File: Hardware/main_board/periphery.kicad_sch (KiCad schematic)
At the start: 66 parts, among them J4 SD, J5 NFC, J6 EXT1, J7 EXT0, U12 LP5562TMX

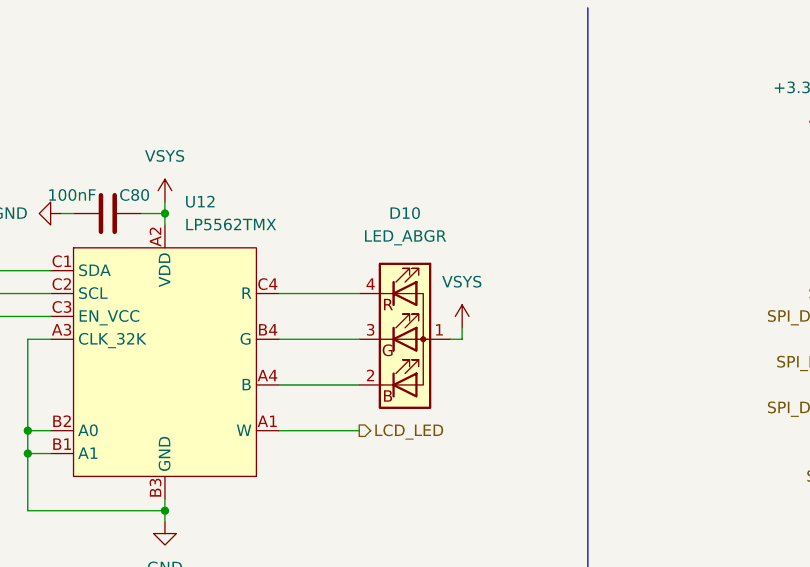
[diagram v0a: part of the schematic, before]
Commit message: layout: change LED footprint
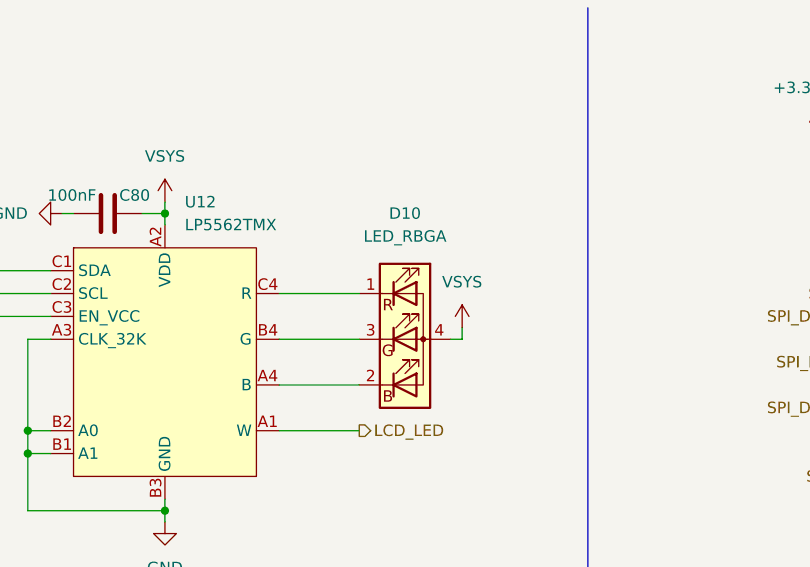
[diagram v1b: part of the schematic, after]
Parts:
- removed D10: LED_ABGR, Library:LED_PLCC-4_1.5x1.5mm_CW, symbol Device:LED_ABGR
- added D10: LED_RBGA, Library:LTST-C19HE1WT_LTO, symbol Device:LED_RBGA
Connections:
- net VSYS: now also D10.4 (A)
- net at U12.A4 (B): now also D10.2 (BK)
- net at U12.B4 (G): now also D10.3 (GK)
- net at U12.C4 (R): now also D10.1 (RK)
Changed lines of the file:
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@@
 	)
 	(symbol
+		(lib_id "Device:LED_RBGA")
+		(at 90.17 49.53 0)
+		(unit 1)
+		(exclude_from_sim no)
+		(in_bom yes)
+		(on_board yes)
+		(dnp no)
+		(fields_autoplaced yes)
+		(property "Reference" "D10"
+			(at 90.17 35.56 0)
+			(effects
+				(font
+					(size 1.27 1.27)
+				)
+			)
+		)
+		(property "Value" "LED_RBGA"
+			(at 90.17 38.1 0)
+			(effects
+				(font
+					(size 1.27 1.27)
+				)
+			)
+		)
+		(property "Footprint" "Library:LTST-C19HE1WT_LTO"
+			(at 90.17 50.8 0)
+			(effects
+				(font
+					(size 1.27 1.27)
+				)
+				(hide yes)
+			)
+		)
+		(property "Datasheet" "~"
+			(at 90.17 50.8 0)
+			(effects
+				(font
+					(size 1.27 1.27)
+				)
+				(hide yes)
+			)
+		)
+		(property "Description" "RGB LED, red/blue/green/anode"
+			(at 90.17 49.53 0)
+			(effects
+				(font
+					(size 1.27 1.27)
+				)
+				(hide yes)
+			)
+		)
+		(pin "1"
+		)
+		(pin "4"
+		)
+		(pin "2"
+		)
+		(pin "3"
+		)
+		(instances
+			(project ""
+				(path "/16216a68-6dea-41d7-8e15-2cc84f72f8e2/07054158-43be-4dab-a684-c4a4bca9b970"
+					(reference "D10")
+					(unit 1)
+				)
+			)
+		)
+	)
+	(symbol
 		(lib_id "Connector:TestPoint")
 		(at 250.19 111.76 0)
@@
 					(unit 1)
 				)
-			)
-		)
-	)
-	(symbol
-		(lib_id "Device:LED_ABGR")
-		(at 90.17 49.53 0)
-		(unit 1)
-		(exclude_from_sim no)
-		(in_bom yes)
-		(on_board yes)
-		(dnp no)
-		(fields_autoplaced yes)
-		(property "Reference" "D10"
-			(at 90.17 35.56 0)
-			(effects
-				(font
-					(size 1.27 1.27)
-				)
-			)
-		)
-		(property "Value" "LED_ABGR"
-			(at 90.17 38.1 0)
-			(effects
-				(font
-					(size 1.27 1.27)
-				)
-			)
-		)
-		(property "Footprint" "Library:LED_PLCC-4_1.5x1.5mm_CW"
-			(at 90.17 50.8 0)
-			(effects
-				(font
-					(size 1.27 1.27)
-				)
-				(hide yes)
-			)
-		)
-		(property "Datasheet" "~"
-			(at 90.17 50.8 0)
-			(effects
-				(font
-					(size 1.27 1.27)
-				)
-				(hide yes)
-			)
-		)
-		(property "Description" "RGB LED, anode/blue/green/red"
-			(at 90.17 49.53 0)
-			(effects
-				(font
-					(size 1.27 1.27)
-				)
-				(hide yes)
-			)
-		)
-		(pin "2"
-		)
-		(pin "4"
-		)
-		(pin "3"
-		)
-		(pin "1"
-		)
-		(instances
-			(project ""
-				(path "/16216a68-6dea-41d7-8e15-2cc84f72f8e2/07054158-43be-4dab-a684-c4a4bca9b970"
-					(reference "D10")
-					(unit 1)
-				)
